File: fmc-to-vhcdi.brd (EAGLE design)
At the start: 76.5 x 69 mm, 16 parts, among them J2 0714300008, J9 FMC_SINGLE_WIDTH_MODULE, U23 24AA64ST

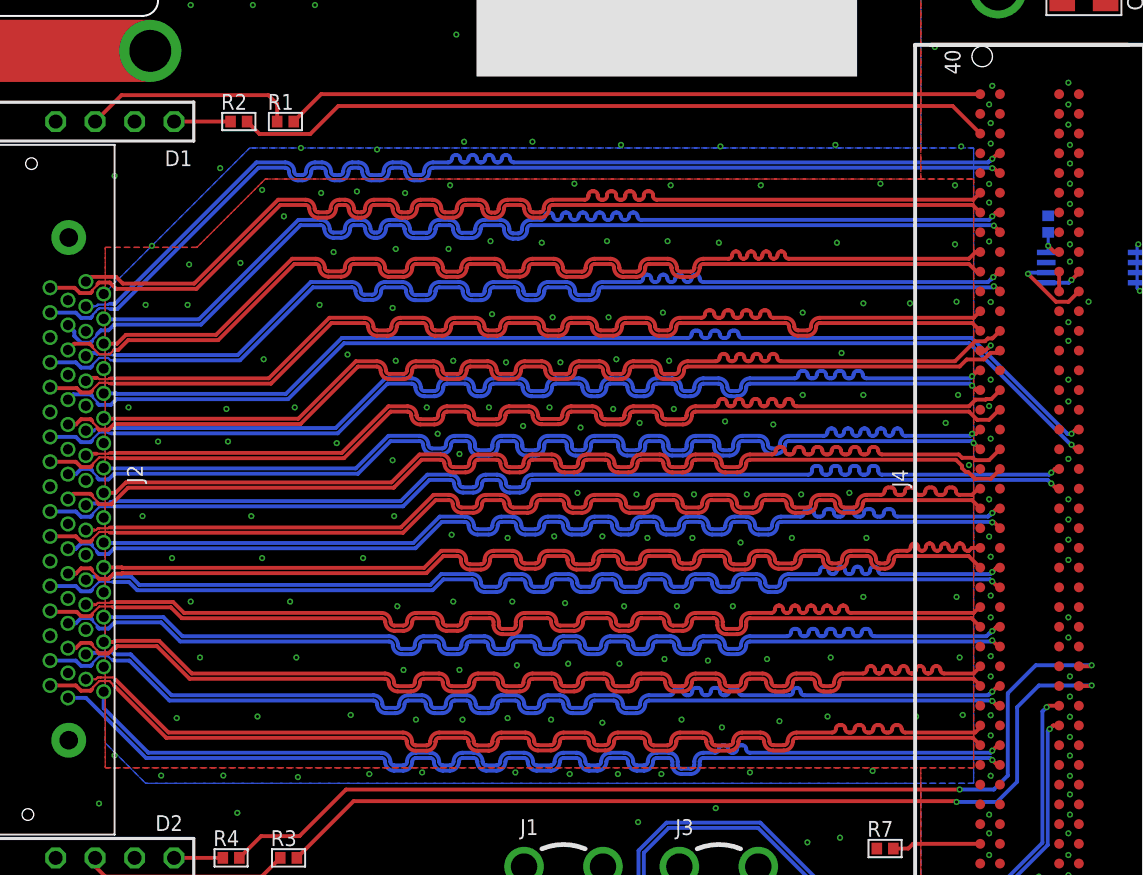
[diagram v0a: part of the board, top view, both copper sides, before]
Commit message: Minor updates to improve trace length equalization
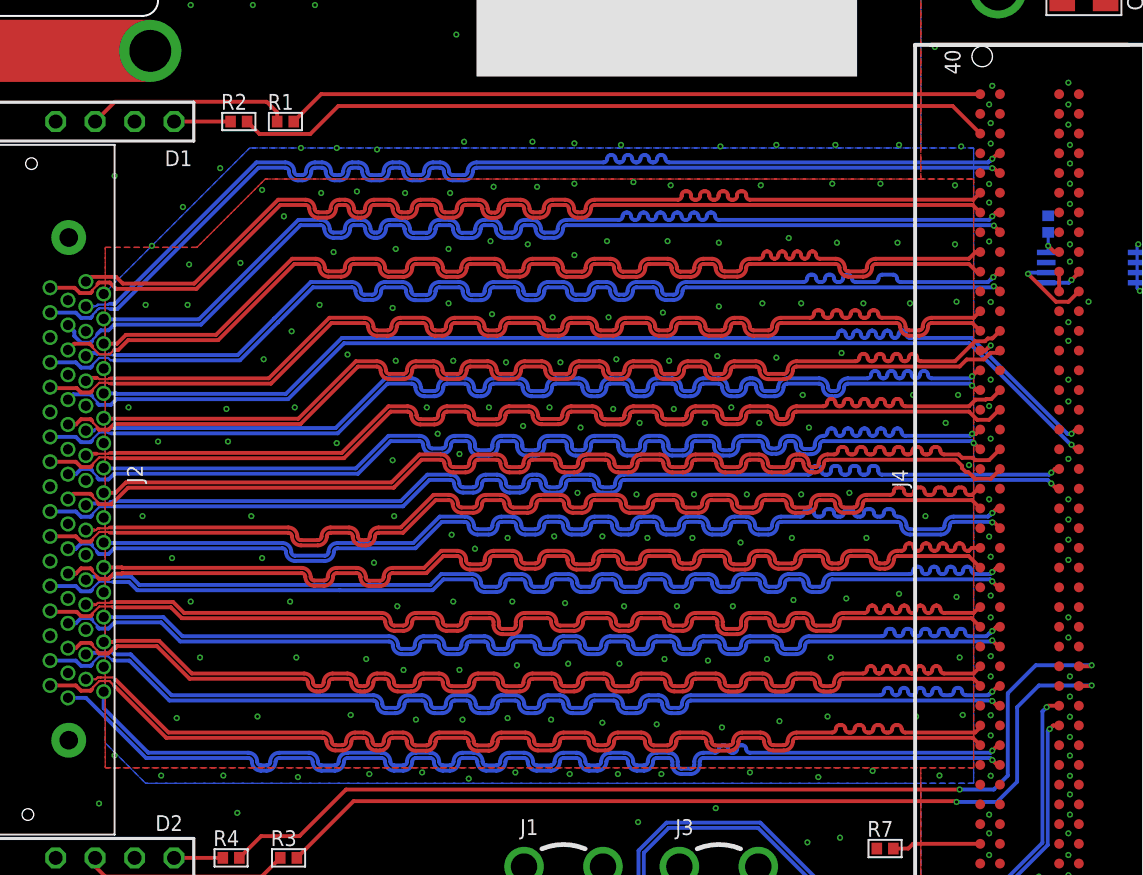
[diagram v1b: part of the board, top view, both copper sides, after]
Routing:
- net DOUT7_LVDS_P: track 66.6 -> 67.9 mm
- net DOUT7_LVDS_N: track 65.1 -> 66.5 mm
- net EX_VALUE_O0_N: track 66.1 -> 67.4 mm
- net EX_IN_2ND_1_LVDS_N: track 65.3 -> 66.7 mm
- net DOUT3_LVDS_N: track 65.6 -> 67.0 mm
- net EX_VALUE_O1_N: track 65.5 -> 66.8 mm
- net DOUT9_LVDS_P: track 66.8 -> 68.2 mm
- net DOUT9_LVDS_N: track 65.7 -> 67.0 mm
- net DOUT8_LVDS_N: track 65.3 -> 66.7 mm
- net VSYNC_LVDS_P: track 66.8 -> 68.1 mm
- net PCLK_LVDS_P: track 67.8 -> 69.2 mm
- net EX_VALUE_O1_P: track 66.6 -> 67.9 mm
- net EX_SHIFT_ENB_LVDS_P: track 66.7 -> 68.0 mm
- net EX_IN_2ND_1_LVDS_P: track 66.7 -> 68.1 mm
- net DOUT1_LVDS_P: track 66.9 -> 68.2 mm
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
